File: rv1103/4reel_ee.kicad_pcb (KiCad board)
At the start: 4 copper layers, 117.5 x 30 mm, 152 parts, among them J1 USB_C_Receptacle_USB2.0_16P, J2 Micro_SD_Card_Det2, J3 RJ45_Hanrun_HR911105A_Horizon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, J4 JST, U1 RV1103G, U2 EA3036C, U3 ImageSensor_OV9281, U4 TLV73312PDBV, U5 TPD2EUSB30, U6 TLV73328PDBV, U7 W25Q32JVZP, U8 LIS2HH12, U9 ImageSensor_OV9281, Y1 TXC-7C, Y2 24Mhz, Y3 TXC-7C

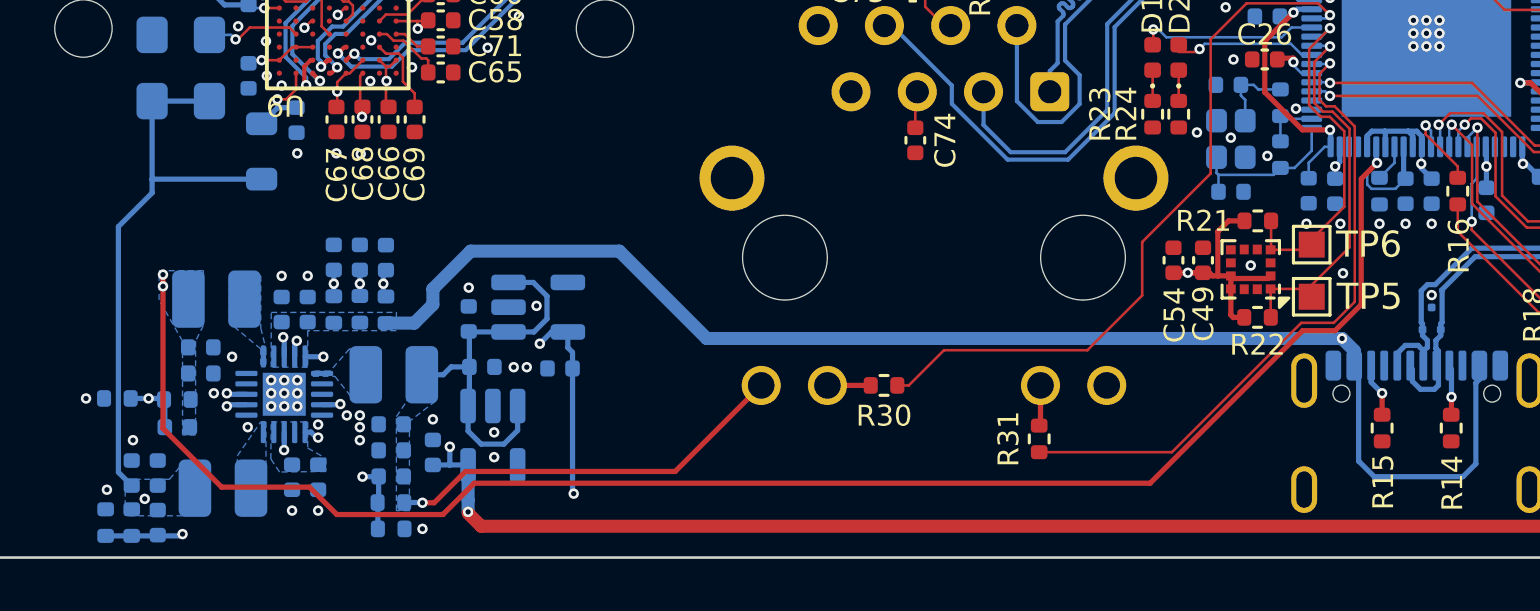
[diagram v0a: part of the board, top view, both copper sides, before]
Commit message: Changed LED resistors size and thicken up 0.9V trace.
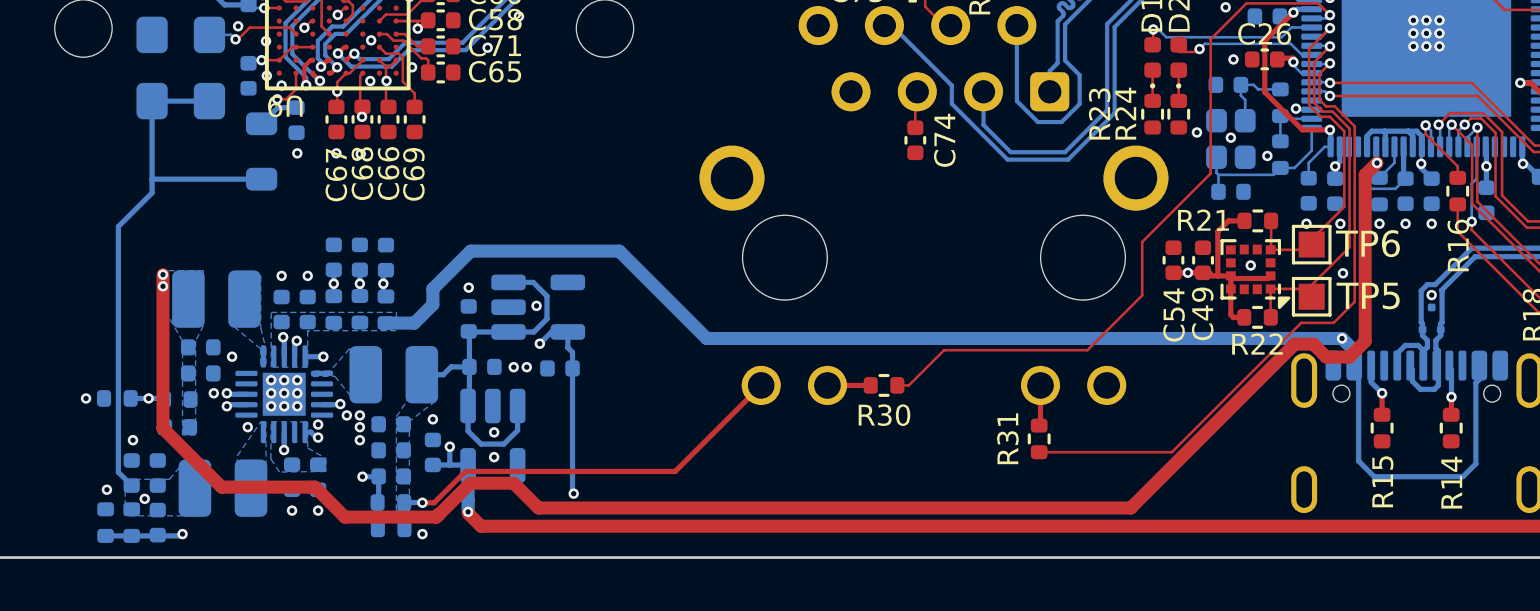
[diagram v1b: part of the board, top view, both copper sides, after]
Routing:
- net +0V9: track 98.9 -> 101.1 mm
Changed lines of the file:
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@@
 	)
 	(via
-		(at 90.2 113.9)
+		(at 90.2 114.1)
 		(size 0.4)
 		(drill 0.2)
@@
 	)
 	(segment
+		(start 123.69651 99.420774)
+		(end 124.675736 100.4)
+		(width 0.2)
+		(layer "In1.Cu")
+		(net "+1V8")
+	)
+	(segment
 		(start 168.2 89.05)
 		(end 134.2225 89.05)
@@
 	)
 	(segment
-		(start 124.675736 100.4)
-		(end 123.69651 99.420774)
+		(start 79.55 113.215686)
+		(end 79.55 112.75)
 		(width 0.2)
 		(layer "In1.Cu")
@@
 	)
 	(segment
-		(start 79.55 113.215686)
-		(end 79.55 112.75)
+		(start 125.55 105.35)
+		(end 124.75 105.35)
 		(width 0.2)
 		(layer "In1.Cu")
@@
 	)
 	(segment
-		(start 125.55 105.35)
-		(end 124.75 105.35)
+		(start 124.675736 100.4)
+		(end 127.7 100.4)
+		(width 0.2)
+		(layer "In1.Cu")
+		(net "+1V8")
+	)
+	(segment
+		(start 128.2 99.9)
+		(end 128.5 99.9)
 		(width 0.2)
 		(layer "In1.Cu")
@@
 	)
 	(segment
-		(start 118 112.1)
-		(end 88.9 112.1)
+		(start 127.7 100.4)
+		(end 128.2 99.9)
 		(width 0.2)
 		(layer "In1.Cu")
@@
 	)
 	(segment
-		(start 132.4 99.9)
-		(end 131.9 100.4)
+		(start 118 112.1)
+		(end 88.9 112.1)
 		(width 0.2)
 		(layer "In1.Cu")
@@
 	)
 	(segment
-		(start 123.69651 99.420774)
-		(end 123.69651 97.786673)
+		(start 132.4 99.9)
+		(end 131.9 100.4)
 		(width 0.2)
 		(layer "In1.Cu")
@@
 	)
 	(segment
-		(start 127.4 99.9)
-		(end 126.9 100.4)
+		(start 123.69651 97.786673)
+		(end 123.69651 99.420774)
 		(width 0.2)
 		(layer "In1.Cu")
@@
 	)
 	(segment
-		(start 126.9 100.4)
-		(end 124.675736 100.4)
-		(width 0.2)
-		(layer "In1.Cu")
-		(net "+1V8")
-	)
-	(segment
 		(start 168.25 89.1)
 		(end 168.2 89.05)
@@
 	(segment
 		(start 128.5 99.9)
-		(end 127.4 99.9)
-		(width 0.2)
-		(layer "In1.Cu")
-		(net "+1V8")
-	)
-	(segment
-		(start 128.5 99.9)
 		(end 128.5 102.4)
 		(width 0.2)
@@
 	)
 	(segment
-		(start 90.984314 113.35)
-		(end 92.184314 112.15)
-		(width 0.2)
+		(start 90.836396 113.35)
+		(end 90.736396 113.45)
+		(width 0.5)
 		(layer "F.Cu")
 		(net "+0V9")
 	)
 	(segment
-		(start 85.865686 112.3)
-		(end 86.915686 113.35)
-		(width 0.2)
+		(start 124.86 107.312918)
+		(end 124.362082 106.815)
+		(width 0.5)
 		(layer "F.Cu")
 		(net "+0V9")
 	)
 	(segment
-		(start 92.184314 112.15)
-		(end 118.103554 112.15)
+		(start 123.6 94.1)
+		(end 122.5 95.2)
 		(width 0.2)
 		(layer "F.Cu")
@@
 	)
 	(segment
-		(start 80.25 110.05)
-		(end 82.5 112.3)
-		(width 0.2)
+		(start 92.036396 112.15)
+		(end 90.836396 113.35)
+		(width 0.5)
 		(layer "F.Cu")
 		(net "+0V9")
 	)
 	(segment
-		(start 125.2 106.3)
-		(end 126.2 105.3)
-		(width 0.2)
+		(start 125.746066 107.312918)
+		(end 124.86 107.312918)
+		(width 0.5)
 		(layer "F.Cu")
 		(net "+0V9")
 	)
 	(segment
-		(start 123.6 94.1)
-		(end 122.5 95.2)
+		(start 122.5 97.155848)
+		(end 123.944151 98.6)
 		(width 0.2)
 		(layer "F.Cu")
@@
 	)
 	(segment
-		(start 86.915686 113.35)
-		(end 90.984314 113.35)
-		(width 0.2)
+		(start 126.35 100.324332)
+		(end 126.35 106.708984)
+		(width 0.5)
 		(layer "F.Cu")
 		(net "+0V9")
 	)
 	(segment
-		(start 122.5 97.155848)
-		(end 123.944151 98.6)
-		(width 0.2)
+		(start 85.865686 112.3)
+		(end 82.5 112.3)
+		(width 0.5)
+		(layer "F.Cu")
+		(net "+0V9")
+	)
+	(segment
+		(start 80.25 110.05)
+		(end 80.25 104.15)
+		(width 0.5)
 		(layer "F.Cu")
 		(net "+0V9")
@@
 	)
 	(segment
+		(start 82.5 112.3)
+		(end 80.25 110.05)
+		(width 0.5)
+		(layer "F.Cu")
+		(net "+0V9")
+	)
+	(segment
 		(start 133.7 92.9)
 		(end 134.27 92.9)
@@
 	)
 	(segment
-		(start 126.2 100.474332)
-		(end 126.804332 99.87)
-		(width 0.2)
+		(start 126.804332 99.87)
+		(end 126.35 100.324332)
+		(width 0.5)
 		(layer "F.Cu")
 		(net "+0V9")
 	)
 	(segment
-		(start 126.2 105.3)
-		(end 126.2 100.474332)
-		(width 0.2)
+		(start 126.35 106.708984)
+		(end 125.746066 107.312918)
+		(width 0.5)
 		(layer "F.Cu")
 		(net "+0V9")
 	)
 	(segment
-		(start 122.5 95.2)
-		(end 122.5 97.155848)
-		(width 0.2)
+		(start 87.227818 113.45)
+		(end 86.077818 112.3)
+		(width 0.5)
 		(layer "F.Cu")
 		(net "+0V9")
 	)
 	(segment
-		(start 82.5 112.3)
+		(start 93.7 112.15)
+		(end 92.036396 112.15)
+		(width 0.5)
+		(layer "F.Cu")
+		(net "+0V9")
+	)
+	(segment
+		(start 123.650686 106.815)
+		(end 117.365686 113.1)
+		(width 0.5)
+		(layer "F.Cu")
+		(net "+0V9")
+	)
+	(segment
+		(start 86.077818 112.3)
 		(end 85.865686 112.3)
-		(width 0.2)
+		(width 0.5)
 		(layer "F.Cu")
 		(net "+0V9")
 	)
 	(segment
-		(start 123.944151 98.6)
-		(end 125 98.6)
-		(width 0.2)
+		(start 117.365686 113.1)
+		(end 94.65 113.1)
+		(width 0.5)
 		(layer "F.Cu")
 		(net "+0V9")
 	)
 	(segment
-		(start 80.25 104.15)
-		(end 80.25 110.05)
-		(width 0.2)
+		(start 90.836396 113.35)
+		(end 90.8 113.35)
+		(width 0.5)
 		(layer "F.Cu")
 		(net "+0V9")
 	)
 	(segment
-		(start 127.763682 89.731311)
-		(end 127.798689 89.731311)
-		(width 0.1)
+		(start 124.362082 106.815)
+		(end 123.650686 106.815)
+		(width 0.5)
 		(layer "F.Cu")
 		(net "+0V9")
 	)
 	(segment
-		(start 123.953554 106.3)
-		(end 125.2 106.3)
+		(start 122.5 95.2)
+		(end 122.5 97.155848)
 		(width 0.2)
 		(layer "F.Cu")
@@
 	)
 	(segment
-		(start 118.103554 112.15)
-		(end 123.953554 106.3)
+		(start 94.65 113.1)
+		(end 93.7 112.15)
+		(width 0.5)
+		(layer "F.Cu")
+		(net "+0V9")
+	)
+	(segment
+		(start 123.944151 98.6)
+		(end 125 98.6)
 		(width 0.2)
 		(layer "F.Cu")
 		(net "+0V9")
+	)
+	(segment
+		(start 90.736396 113.45)
+		(end 87.227818 113.45)
+		(width 0.5)
+		(layer "F.Cu")
+		(net "+0V9")
+	)
+	(segment
+		(start 127.763682 89.731311)
+		(end 127.798689 89.731311)
+		(width 0.1)
+		(layer "F.Cu")
+		(net "+0V9")

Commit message: R0.2 rc
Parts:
- J4: value JST -> SM04B-SRSS-TB
- R23, R24: value 1k -> 470R
- U7: value W25Q32JVZP -> GD25Q128EWIGY
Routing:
- net +3V3: track 177.3 -> 163.6 mm, vias 11 -> 12
- net +5V: track 100.4 -> 96.2 mm, vias 5 -> 7
- net +0V9: track 101.1 -> 99.4 mm
- net /MPU/USB.DN: track 19.6 -> 20.5 mm
- net /Flash/FSPI.D1: track 18.9 -> 18.0 mm
- net /Flash/FSPI.~{CS}: track 21.6 -> 20.7 mm
- net /MPU/USB.DP: track 18.6 -> 19.2 mm
- net GND: vias 244 -> 245

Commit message: Fixed USB-HS routing.
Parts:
- added SYM1: Logo_Open_Hardware_Large, Symbol:OSHW-Logo2_14.6x12mm_SilkScreen, F.Cu at (163.1, 109.4)
- moved U5 0.64 mm to (128.3, 105.5)
- moved H4 0.14 mm to (182.5, 112.0)
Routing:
- net /MPU/USB.DP: track 19.2 -> 21.7 mm, vias 0 -> 2
- net /MPU/USB.DN: track 20.5 -> 21.8 mm, vias 0 -> 2
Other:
- board text added: "Rootkit Labs 4reel RV1103 R0.2"
